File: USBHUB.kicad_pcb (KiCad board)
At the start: 6 copper layers, 89.8 x 89.8 mm, 249 parts, among them J1 USB_C_Receptacle, J2 R-RJ45R08P-C000, J3 Screw_Terminal_01x02, Q1 SI3421DV, Q2 SI3421DV, T1 G24P02S, U1 CYPD3177_24x, U10 USB_3_Type_A_Molex_484080003, U11 CYUSB3304-68LTXx, U12 TPS20xxC, U13 TPS20xxC, U14 TPS20xxC, U15 RTL8153-VB-CG, U2 TPS54331, U3 TLV75733PDBV, U4 TPS56637RPAR, U5 TVS2200DRVx, U6 PI3USB302-Ax, U7 TUSB522Px, U8 USB_3_Type_A_Molex_484080003, U9 USB_3_Type_A_Molex_484080003, Y1 26MHz, Y2 25MHz 18pF

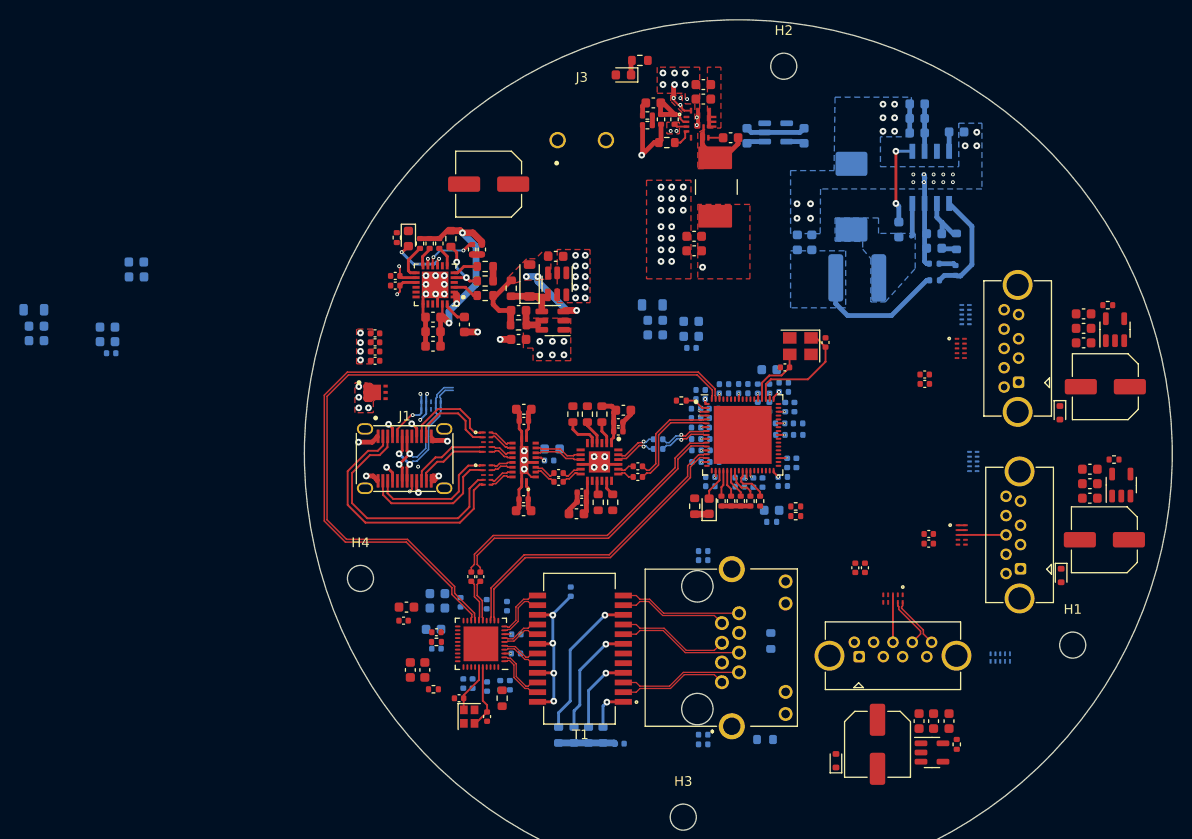
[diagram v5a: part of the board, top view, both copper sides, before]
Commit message: power layout for ethernet usb nic
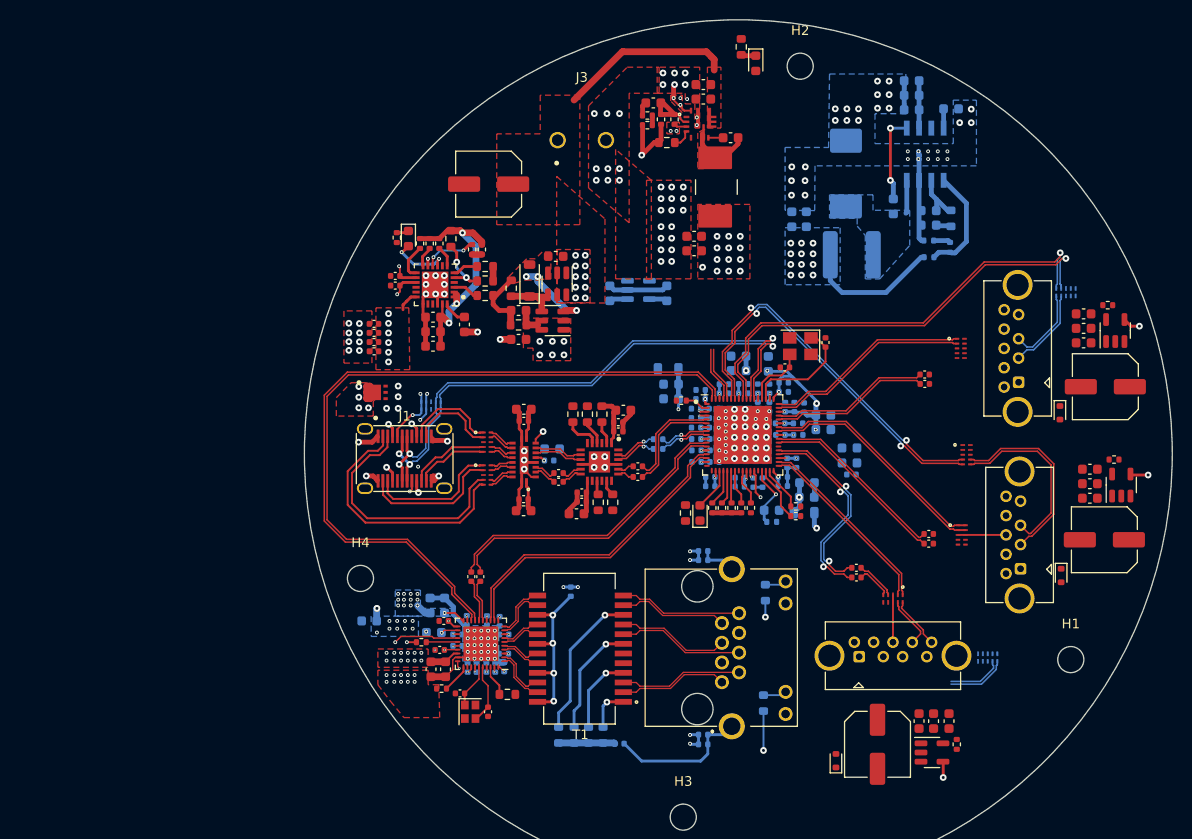
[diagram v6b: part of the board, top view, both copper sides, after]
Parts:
- added C153: 100n, Capacitor_SMD:C_0402_1005Metric, F.Cu at (87.3, 157.8)
- C128, C138: moved to B.Cu
- D13: moved to F.Cu
- moved FB1 82.4 mm to (125.0, 143.6), turned to 180 degrees
- moved C72 81.6 mm to (125.3, 142.0), turned to 0 degrees
- moved C73 81.1 mm to (125.3, 140.5), turned to 0 degrees
- moved C86 74.6 mm to (127.0, 133.5), turned to 0 degrees
- moved C87 74.6 mm to (127.0, 135.0), turned to 0 degrees
- moved C88 71.9 mm to (125.0, 132.7), turned to 90 degrees
- moved C106 63.3 mm to (118.2, 128.9)
- moved C105 62.8 mm to (118.2, 127.4)
- moved C19 21.6 mm to (110.8, 120.9)
- moved C18 21.6 mm to (104.9, 120.9)
- moved U3 21.6 mm to (107.9, 120.5)
- moved C54 21.1 mm to (129.9, 139.7)
- moved C52 21.0 mm to (129.7, 136.9)
- moved C53 21.0 mm to (129.7, 138.4)
- moved D4 13.7 mm to (120.0, 97.1), turned to -90 degrees
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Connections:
- U11 pad 14: HUB1_DS4_RXP -> HUB1_DS4_RXN
- U11 pad 15: HUB1_DS4_RXN -> HUB1_DS4_RXP
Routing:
- net HUB1_PWR_EN_DS: track 0.00 -> 121.8 mm, vias 0 -> 4
- net +1V2: track 22.0 -> 120.8 mm, vias 11 -> 29
- net /05 Ethernet USB IC/LED_R+: track 0.00 -> 61.7 mm, vias 0 -> 2
- net +5V: track 33.3 -> 94.9 mm, vias 2 -> 26
- net HUB1_DS2_DN: track 0.00 -> 59.9 mm, vias 0 -> 2
- net HUB1_DS2_DP: track 0.00 -> 58.5 mm, vias 0 -> 2
- net HUB1_DS1_DP: track 0.00 -> 55.6 mm, vias 0 -> 1
- net HUB1_DS1_DN: track 0.00 -> 55.6 mm, vias 0 -> 1
- net /05 Ethernet USB IC/LED_L+: track 0.00 -> 50.8 mm, vias 0 -> 2
- net USB_UFP_DN: track 15.9 -> 58.6 mm, vias 2 -> 3
- net USB_UFP_DP: track 15.8 -> 58.1 mm, vias 2 -> 3
- net /04 Hub Controller/DVDD12: track 3.11 -> 38.2 mm, vias 4 -> 5
- net GND: track 84.5 -> 112.1 mm, vias 84 -> 186
- net USB_UFP_FLIP: track 5.46 -> 30.1 mm, vias 2 -> 3
- net HUB1_DS2_RXP: track 0.77 -> 24.2 mm
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- added copper zone on In2.Cu, net +1V2
- added copper zone on B.Cu, net +5V
- added copper zone on In2.Cu, net +5V
- added copper zone on F.Cu, net /05 Ethernet USB IC/VDD10
- added copper zone on In2.Cu, net /05 Ethernet USB IC/VDD10
- added copper zone on B.Cu, net /05 Ethernet USB IC/VDD33
- added copper zone on In2.Cu, net /05 Ethernet USB IC/VDD33

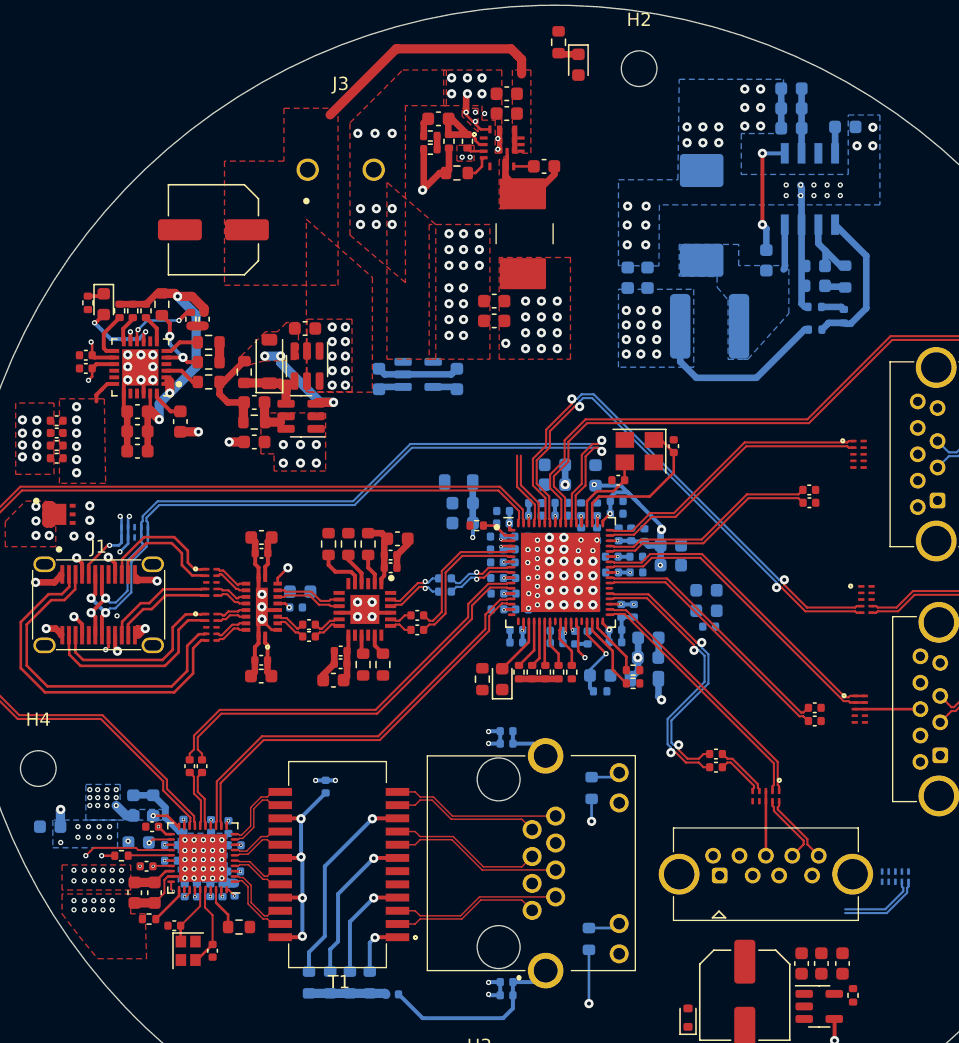
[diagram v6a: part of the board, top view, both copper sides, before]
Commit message: add schottky for usb pd
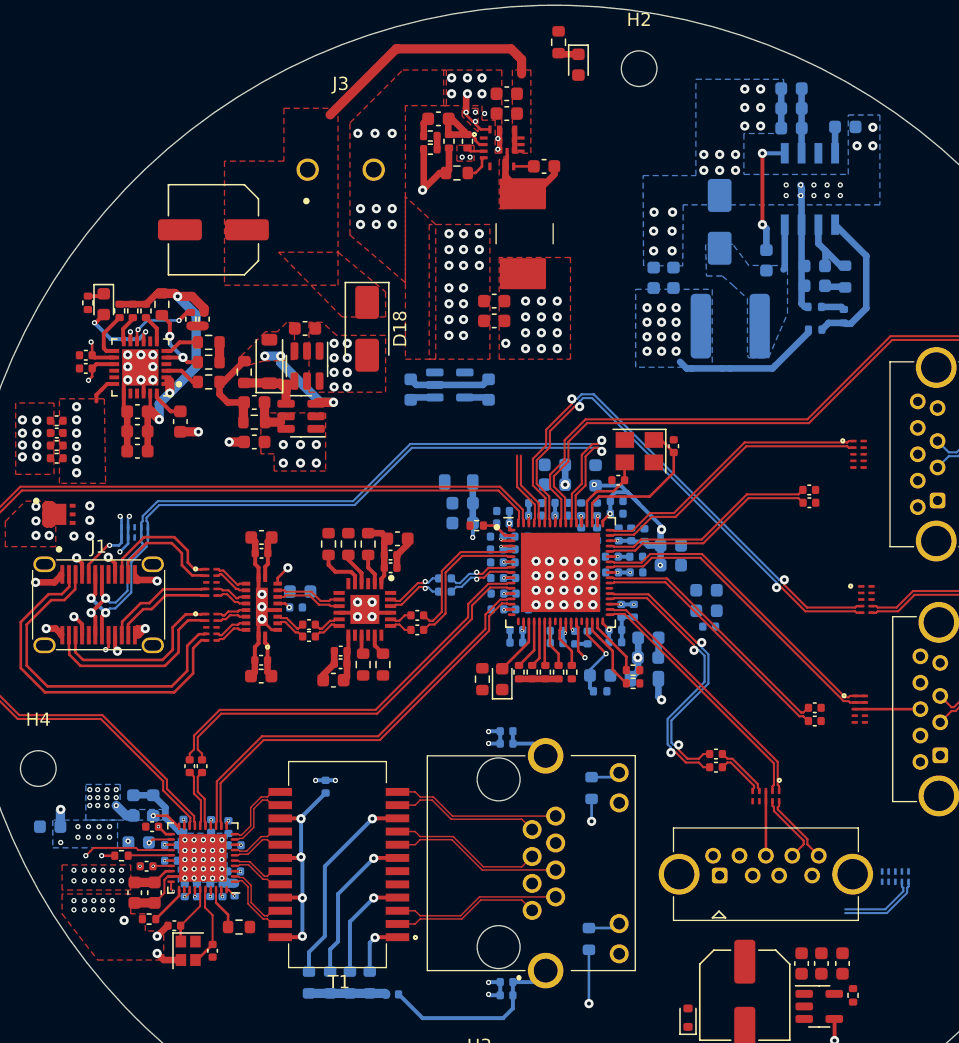
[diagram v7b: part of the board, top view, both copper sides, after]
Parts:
- added D18: SS54, Diode_SMD:D_SMA, F.Cu at (104.0, 117.1)
- D3: value B340 -> Schottky; footprint Diode_SMD:D_SMC -> Diode_SMD:D_SMA
- moved C19 2.53 mm to (113.2, 121.7)
- moved U3 2.53 mm to (110.3, 121.3)
- moved C18 2.53 mm to (107.3, 121.7)
- moved C10 1.97 mm to (125.7, 113.2)
- moved C11 1.97 mm to (127.2, 113.2)
- moved L1 1.57 mm to (131.5, 116.9)
- moved D3 1.45 mm to (130.7, 109.0)
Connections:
- C3 pad 1: +20V -> USB_PD_20V
- Q2 pad 1: +20V -> USB_PD_20V
- Q2 pad 2: +20V -> USB_PD_20V
- Q2 pad 5: +20V -> USB_PD_20V
- Q2 pad 6: +20V -> USB_PD_20V
- U1 pad 11: +20V -> USB_PD_20V
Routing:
- net USB_PD_20V: track 0.00 -> 18.3 mm, vias 0 -> 9
- net +20V: track 35.6 -> 18.0 mm, vias 11 -> 0
- net +1V2: track 120.8 -> 114.7 mm
- net GND: track 112.1 -> 115.4 mm, vias 186 -> 171
- net Net-(D3-K): track 4.54 -> 3.44 mm
- added copper zone on F.Cu, net USB_PD_20V
- added copper zone on In2.Cu, net USB_PD_20V

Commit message: finish layout draft
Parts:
- C18, C19, U3: moved to F.Cu
- moved C53 22.6 mm to (108.2, 131.4)
- moved C52 22.6 mm to (108.2, 129.9)
- moved C54 22.2 mm to (108.8, 132.6)
- moved C18 19.7 mm to (123.5, 110.7), turned to 180 degrees
- moved U3 15.1 mm to (123.2, 113.6), turned to -90 degrees
- moved C19 11.6 mm to (123.5, 116.5), turned to 180 degrees
- moved D17 6.49 mm to (130.0, 163.0), turned to 180 degrees
- moved D4 4.51 mm to (119.7, 101.6)
- moved R22 4.51 mm to (118.2, 99.9)
- moved C70 3.67 mm to (134.7, 145.0), turned to -45 degrees
- moved C82 3.61 mm to (127.8, 147.8), turned to -90 degrees
- moved C111 3.13 mm to (120.1, 129.5), turned to 90 degrees
- moved C71 2.92 mm to (135.4, 144.3), turned to -45 degrees
- moved C101 2.86 mm to (112.8, 133.8), turned to 180 degrees
- moved C105 2.83 mm to (115.6, 128.3), turned to -90 degrees
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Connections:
- D11 pad 1: unconnected-(D11-CH1-Pad1) -> HUB1_DS3_DN
- D11 pad 2: unconnected-(D11-CH2-Pad2) -> HUB1_DS3_DP
- D11 pad 4: HUB1_DS3_DN -> unconnected-(D11-CH3-Pad4)
- D11 pad 5: HUB1_DS3_DP -> unconnected-(D11-CH4-Pad5)
- U11 pad 14: HUB1_DS4_RXN -> HUB1_DS4_RXP
- U11 pad 15: HUB1_DS4_RXP -> HUB1_DS4_RXN
- U3 pad 4: unconnected-(U3-NC-Pad4) -> GND
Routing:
- net +5V: track 94.9 -> 241.9 mm, vias 26 -> 71
- net GND: track 115.4 -> 259.3 mm, vias 171 -> 357
- net +3V3: track 37.2 -> 158.0 mm, vias 6 -> 52
- net HUB1_DS3_DN: track 11.5 -> 85.1 mm, vias 0 -> 2
- net HUB1_DS3_DP: track 11.9 -> 85.1 mm, vias 0 -> 2
- net /03 USB_DFP/USB_DS1_VBUS: track 0.00 -> 17.3 mm
- net +1V2: track 114.7 -> 130.8 mm, vias 29 -> 36
- net /03 USB_DFP/USB_DS2_VBUS: track 0.00 -> 15.6 mm
- net /03 USB_DFP/USB_DS3_VBUS: track 0.00 -> 15.1 mm
- net /04 Hub Controller/DVDD12: track 38.2 -> 52.3 mm
- net /05 Ethernet USB IC/ETH2-: track 0.00 -> 13.3 mm, vias 0 -> 1
- net /05 Ethernet USB IC/ETH2+: track 0.00 -> 13.3 mm, vias 0 -> 1
- net HUB1_DS2_TXN: track 0.00 -> 12.8 mm
- net HUB1_DS2_TXP: track 0.00 -> 12.8 mm
- net HUB1_DS1_TXN: track 0.00 -> 12.4 mm
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- added copper zone on B.Cu, net +3V3
- added copper zone on F.Cu, net +3V3
- added copper zone on In2.Cu, net +3V3
- added copper zone on In4.Cu, net GND
